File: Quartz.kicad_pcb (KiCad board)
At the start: 6 copper layers, 254 x 130 mm, 1244 parts, among them J1 DB37, J2 DB37, J4 Conn_02x10_Odd_Even, J5 PPS IN, J6 WP Jumper, J7 WP Jumper, K1001 EE2-12TNU-L, K101 EE2-12TNU-L, K1101 EE2-12TNU-L, K1201 EE2-12TNU-L, K1301 EE2-12TNU-L, K1401 EE2-12TNU-L, K1501 EE2-12TNU-L, K1601 EE2-12TNU-L, K1701 EE2-12TNU-L, K1801 EE2-12TNU-L, K1901 EE2-12TNU-L, K2001 EE2-12TNU-L, K201 EE2-12TNU-L, K2101 EE2-12TNU-L, K2201 EE2-12TNU-L, K2301 EE2-12TNU-L, K2401 EE2-12TNU-L, K2501 EE2-12TNU-L, K2601 EE2-12TNU-L, K2701 EE2-12TNU-L, K2801 EE2-12TNU-L, K2901 EE2-12TNU-L, K3001 EE2-12TNU-L, K301 EE2-12TNU-L, K3101 EE2-12TNU-L, K3201 EE2-12TNU-L, K401 EE2-12TNU-L, K501 EE2-12TNU-L, K601 EE2-12TNU-L, K701 EE2-12TNU-L, K801 EE2-12TNU-L, K901 EE2-12TNU-L, P1 ASP-134604-01, P2 ASP-134604-01, Q1 FDN335N, Q2 FDN335N, Q3 FDMC510P, U1 AD7768, U10 AD7768, U1001 INA851, U101 INA851, U11 ADR4520, U1101 INA851, U12 ADA4841-1, U1201 INA851, U13 AMC7823, U1301 INA851, U14 MAX4896, U1401 INA851, U15 MAX4896, U1501 INA851, U16 SI5330B-B00205-GM, U1601 INA851, U17 MAX4896, U1701 INA851, U18 MAX4896, U1801 INA851, U19 MAX4896, U1901 INA851, U2 ADR4520, U20 MAX4896, U2001 INA851, U201 INA851, U21 MAX4896, U2101 INA851, U2201 INA851, U23 MAX4896, U2301 INA851, U2401 INA851, U2501 INA851, U26 74AVC4T245, U2601 INA851, U27 AT24C64D, U2701 INA851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

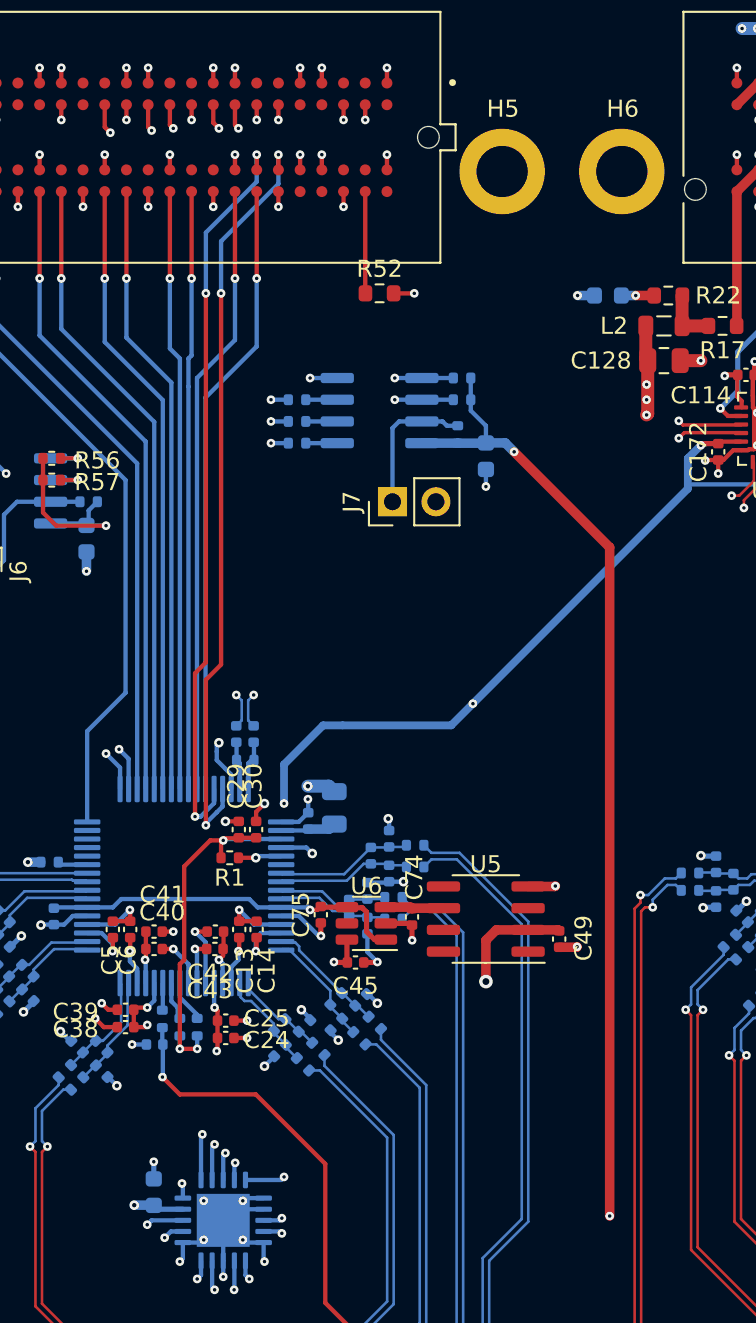
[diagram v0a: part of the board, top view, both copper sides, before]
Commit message: Changed Cal EEPROM to run off 2.5V
Changed Cal EEPROM to run off 2.5V
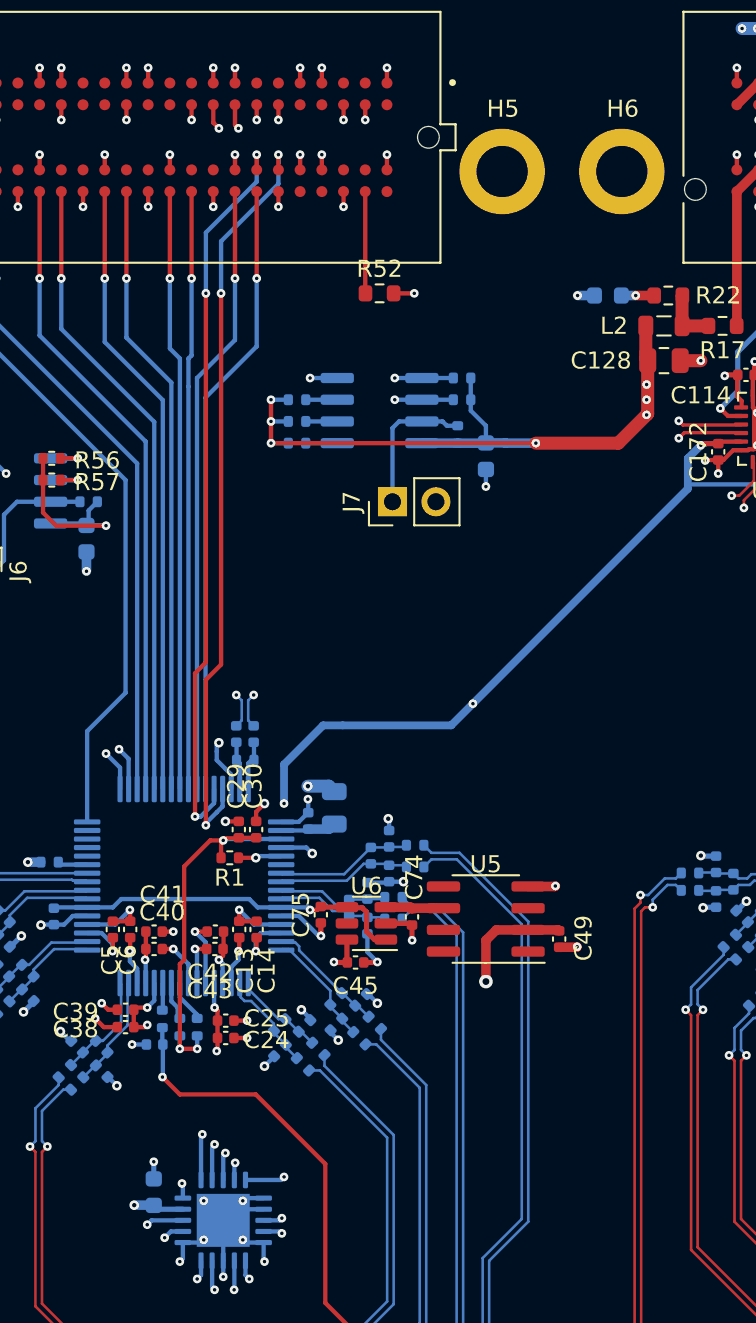
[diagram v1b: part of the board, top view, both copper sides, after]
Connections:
- C132 pad 1: VDD3P3V -> P2_2P5V
- P1 pad D11: CAL_EEPROM_A2 -> unconnected-(P1-PadD11)
- P1 pad D12: CAL_EEPROM_A1 -> unconnected-(P1-PadD12)
- P1 pad D14: CAL_EEPROM_A0 -> unconnected-(P1-PadD14)
- R121 pad 1: CAL_EEPROM_A0 -> P2_2P5V
- R122 pad 1: CAL_EEPROM_A1 -> P2_2P5V
- R123 pad 1: CAL_EEPROM_A2 -> P2_2P5V
- R125 pad 1: VDD3P3V -> P2_2P5V
- R126 pad 1: VDD3P3V -> P2_2P5V
- R127 pad 1: VDD3P3V -> P2_2P5V
- U28 pad 8: VDD3P3V -> P2_2P5V
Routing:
- net VDD3P3V: track 280.6 -> 223.8 mm, vias 22 -> 20
- net P2_2P5V: track 228.5 -> 267.6 mm, vias 17 -> 21
- net CAL_EEPROM_A0: track 27.3 -> 0.00 mm, vias 2 -> 0
- net CAL_EEPROM_A1: track 24.5 -> 0.00 mm, vias 2 -> 0
- net CAL_EEPROM_A2: track 22.3 -> 0.00 mm, vias 2 -> 0
